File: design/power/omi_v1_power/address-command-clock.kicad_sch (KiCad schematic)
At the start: 8 parts

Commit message: feat(phase5): resolve unconnected DRAM balls - genuine NC flags + VSS ties
Per the datasheet-backed classification (1Rx8 non-ECC, non-3DS, DM enabled,
C/A parity disabled): no_connect flags on the genuinely-unused balls A3 (TDQS_c,
DM enabled), F2/G2/G8 (3DS stack-ID + 2nd-rank C0/C1/C2/CKE1/CS1/ODT1), L9
(ALERT, open-drain error output unused in v1) = 40 flags; and global-label VSS
ties on G9 (TEN, test-enable input held low) + N3 (PAR, unused C/A-parity input
tied low rather than floated) = 16 ties (TEN/PAR verified now on GND).

Honest dispositions only: nothing a functional module would connect is silenced.
ERC 85 -> 13 (the 8 ZQ + 5 power remain, resolved next). Netlist parses.

Co-Authored-By: Claude Opus 4.8 (1M context) <noreply@anthropic.com>
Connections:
- net GND: now also U_DRAM0.G9 (TEN), U_DRAM0.N3 (PAR), U_DRAM1.G9 (TEN), U_DRAM1.N3 (PAR), U_DRAM2.G9 (TEN), U_DRAM2.N3 (PAR), U_DRAM3.G9 (TEN), U_DRAM3.N3 (PAR), U_DRAM4.G9 (TEN), U_DRAM4.N3 (PAR), U_DRAM5.G9 (TEN), U_DRAM5.N3 (PAR), U_DRAM6.G9 (TEN), U_DRAM6.N3 (PAR), U_DRAM7.G9 (TEN), U_DRAM7.N3 (PAR)
- no-connect marks 0 -> 40

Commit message: feat(phase5): add the 8 mandatory ZQ calibration resistors (240 ohm to VSS)
JEDEC requires a 240 ohm +/-1% RZQ resistor from each DDR4 device ZQ ball (B9)
to VSS for output-driver/ODT calibration; the design had none (a real defect,
never to be NC-flagged). Add R1-R8 (Device:R, value 240, footprint
Resistor_SMD:R_0402_1005Metric -> preserves 100% footprint coverage), each
wired ZQ(DRAMn) <-> R <-> GND via per-device ZQn global labels (verified
ZQ0={R1,U_DRAM0}). On the 1.27mm grid. ERC 13 -> 5 (power only remains).

Co-Authored-By: Claude Opus 4.8 (1M context) <noreply@anthropic.com>
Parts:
- added R1, R2, R3, R4, R5, R6, R7, R8: 240, Resistor_SMD:R_0402_1005Metric, symbol Device:R
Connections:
- net GND: now also R1.2, R2.2, R3.2, R4.2, R5.2, R6.2, R7.2, R8.2
- net ZQ7: now reaches U_DRAM7.B9 (ZQ)
- net ZQ7: now also R8.1
- net ZQ3: now reaches U_DRAM3.B9 (ZQ)
- net ZQ3: now also R4.1
- net ZQ2: now reaches U_DRAM2.B9 (ZQ)
- net ZQ2: now also R3.1
- net ZQ4: now reaches U_DRAM4.B9 (ZQ)
- net ZQ4: now also R5.1
- net ZQ5: now reaches U_DRAM5.B9 (ZQ)
- net ZQ5: now also R6.1
- net ZQ1: now reaches U_DRAM1.B9 (ZQ)
- net ZQ1: now also R2.1
- net ZQ0: now reaches U_DRAM0.B9 (ZQ)
- net ZQ0: now also R1.1
- net ZQ6: now reaches U_DRAM6.B9 (ZQ)
- net ZQ6: now also R7.1

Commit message: feat(phase5): power drive - VDDQ->VDD merge + PWR_FLAGs (ERC -> 0)
VDDQ: the local /address-command-clock/VDDQ net (48 DRAM VDDQ balls) had no
source and no J1 pin (a DDR4 edge has VDD, not VDDQ). Merge it into VDD by
relabeling the 8 VDDQ locals to global VDD (on a DDR4 UDIMM VDD==VDDQ, bridged
on-module) -> VDD now 139 nodes. PWR_FLAGs: J1 is the off-board power source but
its many same-rail pins cannot all be power_output (would multi-drive-conflict;
a directional retype also broke J1's label-on-pin connectivity, verified +
reverted). So one PWR_FLAG per rail (VDD/VPP/GND/VDDSPD) marks the supply, each
via a wire (driver pins need a wire, not a label-on-pin). ERC 5 -> 0 honestly.

Co-Authored-By: Claude Opus 4.8 (1M context) <noreply@anthropic.com>
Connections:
- net VDDQ is gone; now on net VDD: U_DRAM0.B2 (VDDQ), U_DRAM0.B8 (VDDQ), U_DRAM0.C1 (VDDQ), U_DRAM0.C9 (VDDQ), U_DRAM0.E2 (VDDQ), U_DRAM0.E8 (VDDQ), U_DRAM1.B2 (VDDQ), U_DRAM1.B8 (VDDQ), U_DRAM1.C1 (VDDQ), U_DRAM1.C9 (VDDQ), U_DRAM1.E2 (VDDQ), U_DRAM1.E8 (VDDQ), U_DRAM2.B2 (VDDQ), U_DRAM2.B8 (VDDQ), U_DRAM2.C1 (VDDQ), U_DRAM2.C9 (VDDQ), U_DRAM2.E2 (VDDQ), U_DRAM2.E8 (VDDQ), U_DRAM3.B2 (VDDQ), U_DRAM3.B8 (VDDQ), U_DRAM3.C1 (VDDQ), U_DRAM3.C9 (VDDQ), U_DRAM3.E2 (VDDQ), U_DRAM3.E8 (VDDQ), U_DRAM4.B2 (VDDQ), U_DRAM4.B8 (VDDQ), U_DRAM4.C1 (VDDQ), U_DRAM4.C9 (VDDQ), U_DRAM4.E2 (VDDQ), U_DRAM4.E8 (VDDQ), U_DRAM5.B2 (VDDQ), U_DRAM5.B8 (VDDQ), U_DRAM5.C1 (VDDQ), U_DRAM5.C9 (VDDQ), U_DRAM5.E2 (VDDQ), U_DRAM5.E8 (VDDQ), U_DRAM6.B2 (VDDQ), U_DRAM6.B8 (VDDQ), U_DRAM6.C1 (VDDQ), U_DRAM6.C9 (VDDQ), U_DRAM6.E2 (VDDQ), U_DRAM6.E8 (VDDQ), U_DRAM7.B2 (VDDQ), U_DRAM7.B8 (VDDQ), U_DRAM7.C1 (VDDQ), U_DRAM7.C9 (VDDQ), U_DRAM7.E2 (VDDQ), U_DRAM7.E8 (VDDQ)

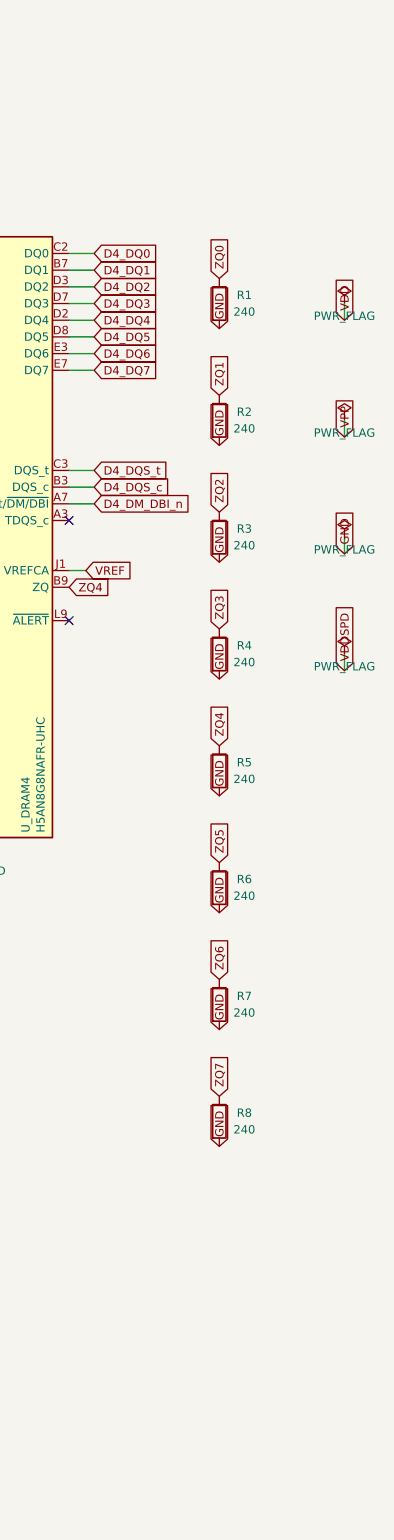
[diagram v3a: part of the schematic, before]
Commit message: polish(schematic): v1.1.0 title blocks + sheet annotations (no electrical change)
Hand-done KiCad 9 GUI pass over all five schematic sheets. Title-block
and text-box content only — no wiring, no component, no net changes.

- Title block (all sheets): Company=OMI, Rev=1.1.0, Date=2026-06-02,
  plus functional per-sheet titles.
- Repurposed the previously-empty DQ/DQS sheet into a byte-lane reference table.
- Added a mechanical caveat text box on the edge (UDIMM) sheet.
- Added a power-rail summary text box on the root sheet.
- omi_v1_power.kicad_prl: project-local UI state saved with the GUI session.

Electrical integrity is asserted to be unchanged and is verified downstream
by the export pipeline (ERC=0 gate + byte-identical netlist and BOM).

Co-Authored-By: Claude Opus 4.8 (1M context) <noreply@anthropic.com>
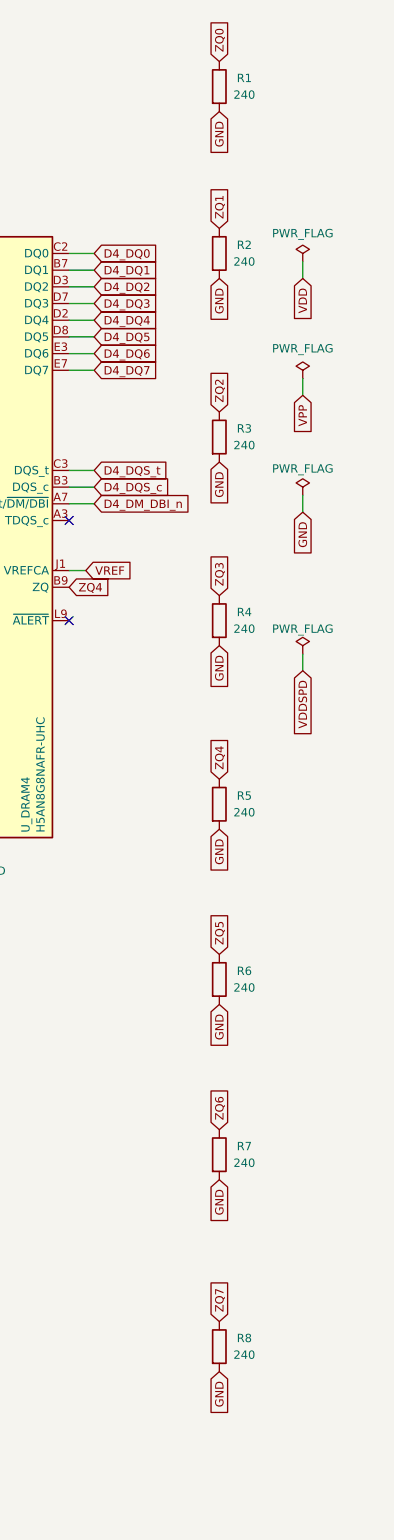
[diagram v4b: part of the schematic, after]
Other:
- title: Stage 7.2 - Address / Command / Clock -> Address / Command / Clock
- moved on the sheet: R1, R2, R3, R4, R5, R6, R7, R8
